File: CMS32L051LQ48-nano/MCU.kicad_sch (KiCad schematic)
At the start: 11 parts, among them J101 Board Pin, J102 Board Pin, U201 CMS32L051LQ48

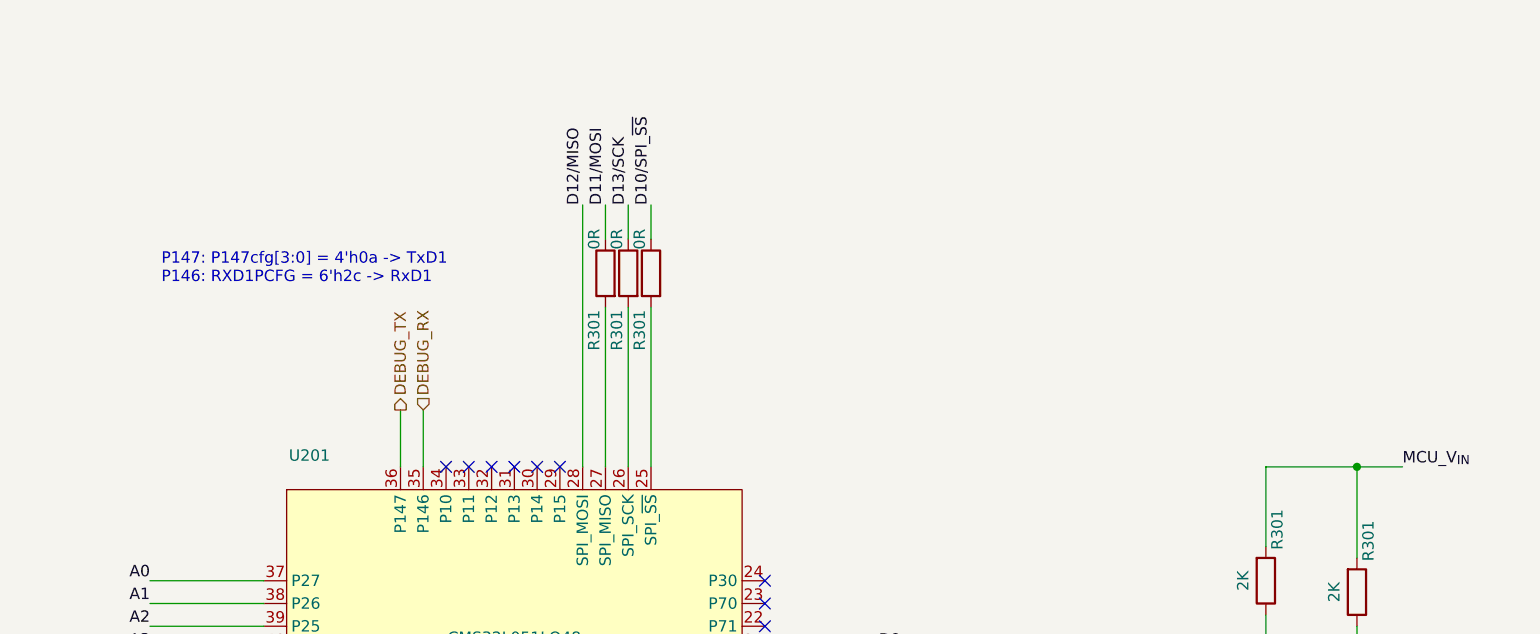
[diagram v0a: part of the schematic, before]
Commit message: added two LEDs
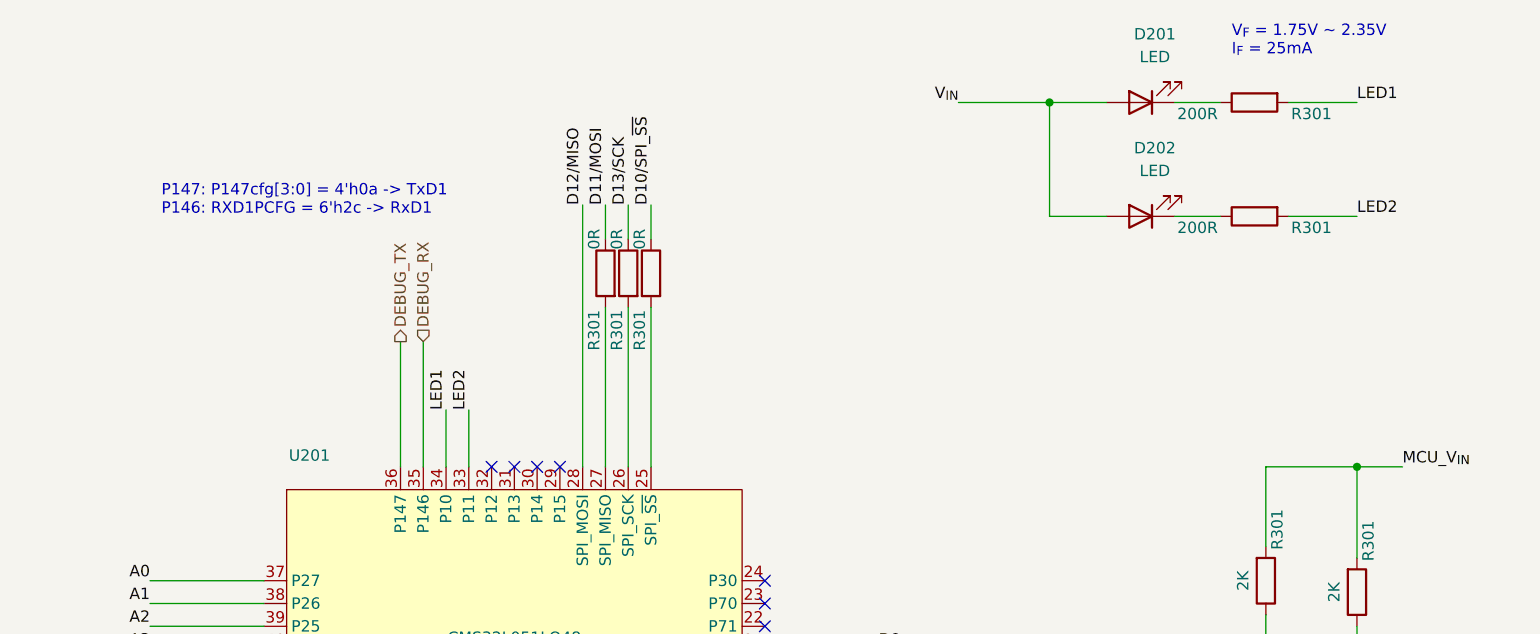
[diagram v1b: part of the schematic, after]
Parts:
- added D201, D202: LED, LED_SMD:LED_0402_1005Metric, symbol Device:LED
- added R301 (x2): 200R, Resistor_SMD:R_0402_1005Metric, symbol Device:R
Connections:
- net V_{IN}: now also D201.2 (A), D202.2 (A)
- net LED2: now reaches U201.33 (P11)
- net LED2: now also R301.2
- net LED1: now reaches U201.34 (P10)
- net LED1: now also R301.2
- new net: D201.1 (K), R301.1
- new net: D202.1 (K), R301.1
- no-connect marks 20 -> 18
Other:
- note added: "V_{F} = 1.75V ~ 2.35V I_{F} = 25mA"
